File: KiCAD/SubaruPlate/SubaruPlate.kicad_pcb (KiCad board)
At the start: 2 copper layers, 140 x 140 mm, 6 parts, among them J1 Conn_01x04, U1 LPS28DFW

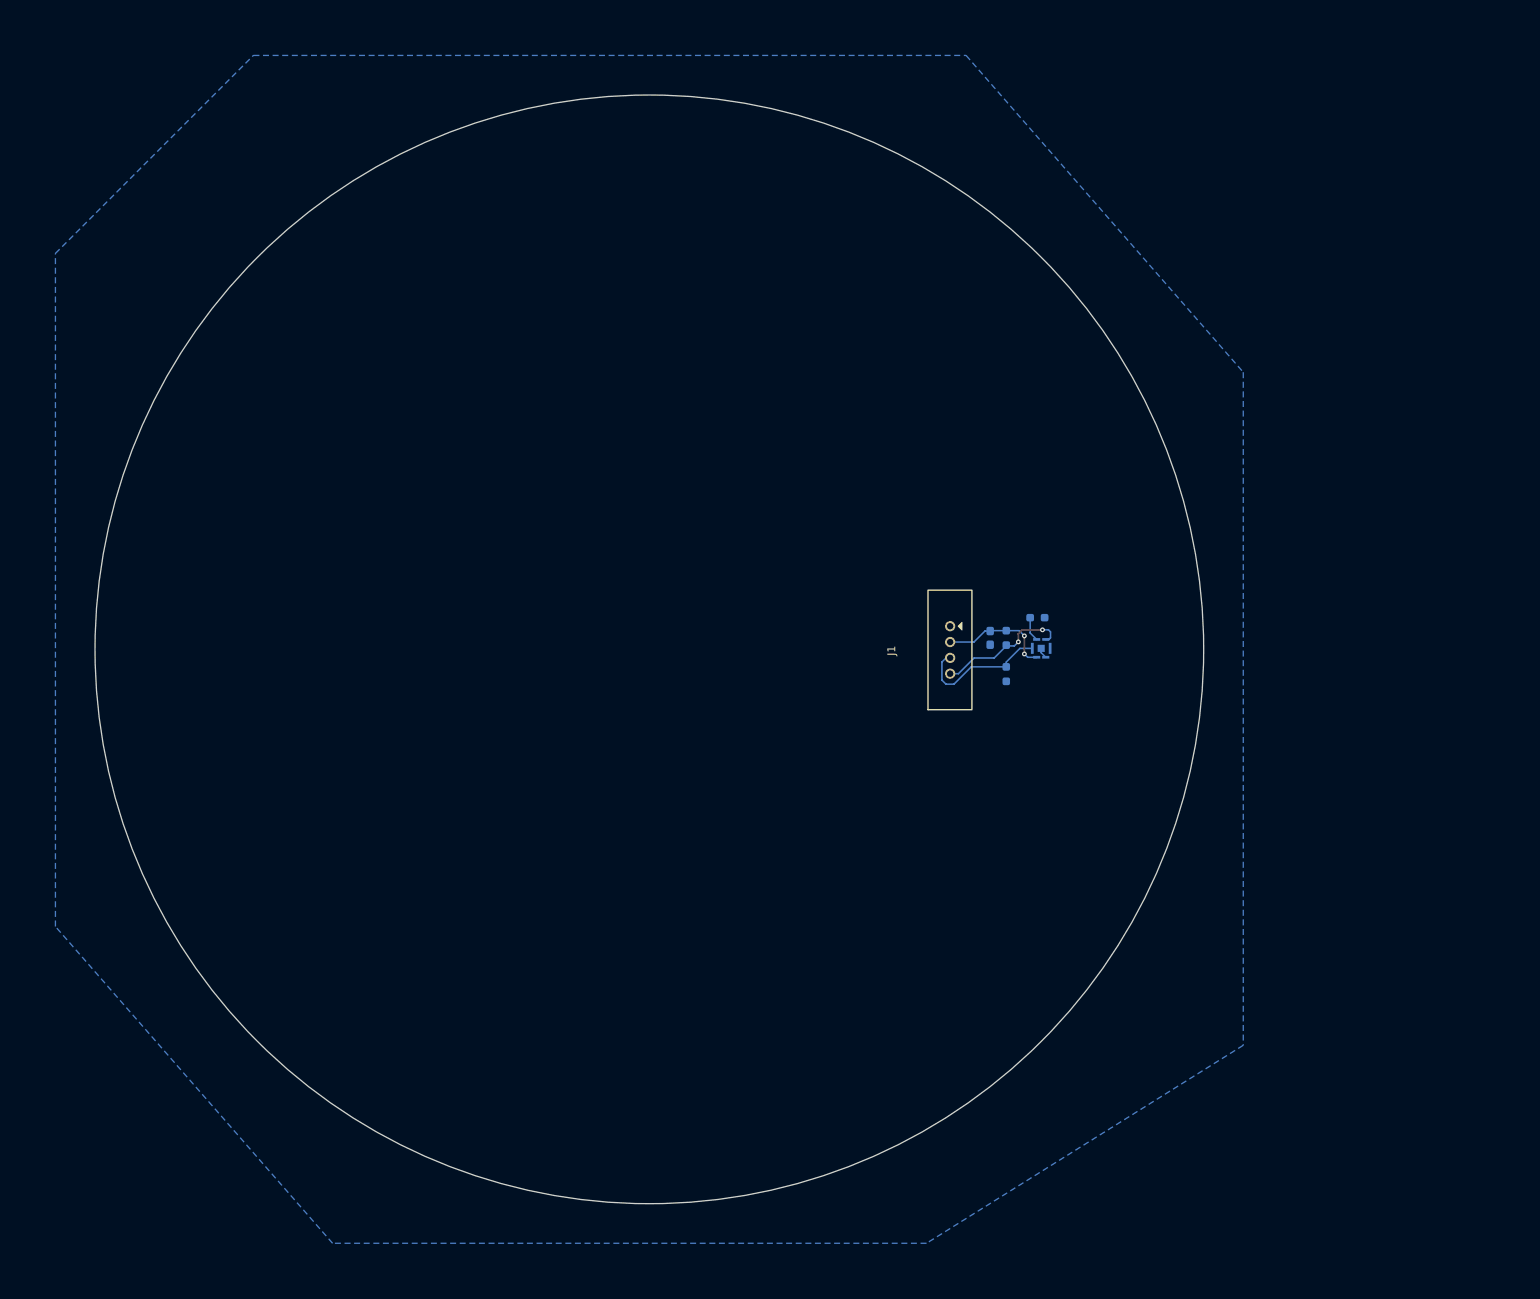
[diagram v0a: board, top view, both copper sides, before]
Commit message: Power, CanInterface, MCU, Sensorと項目に分け設計
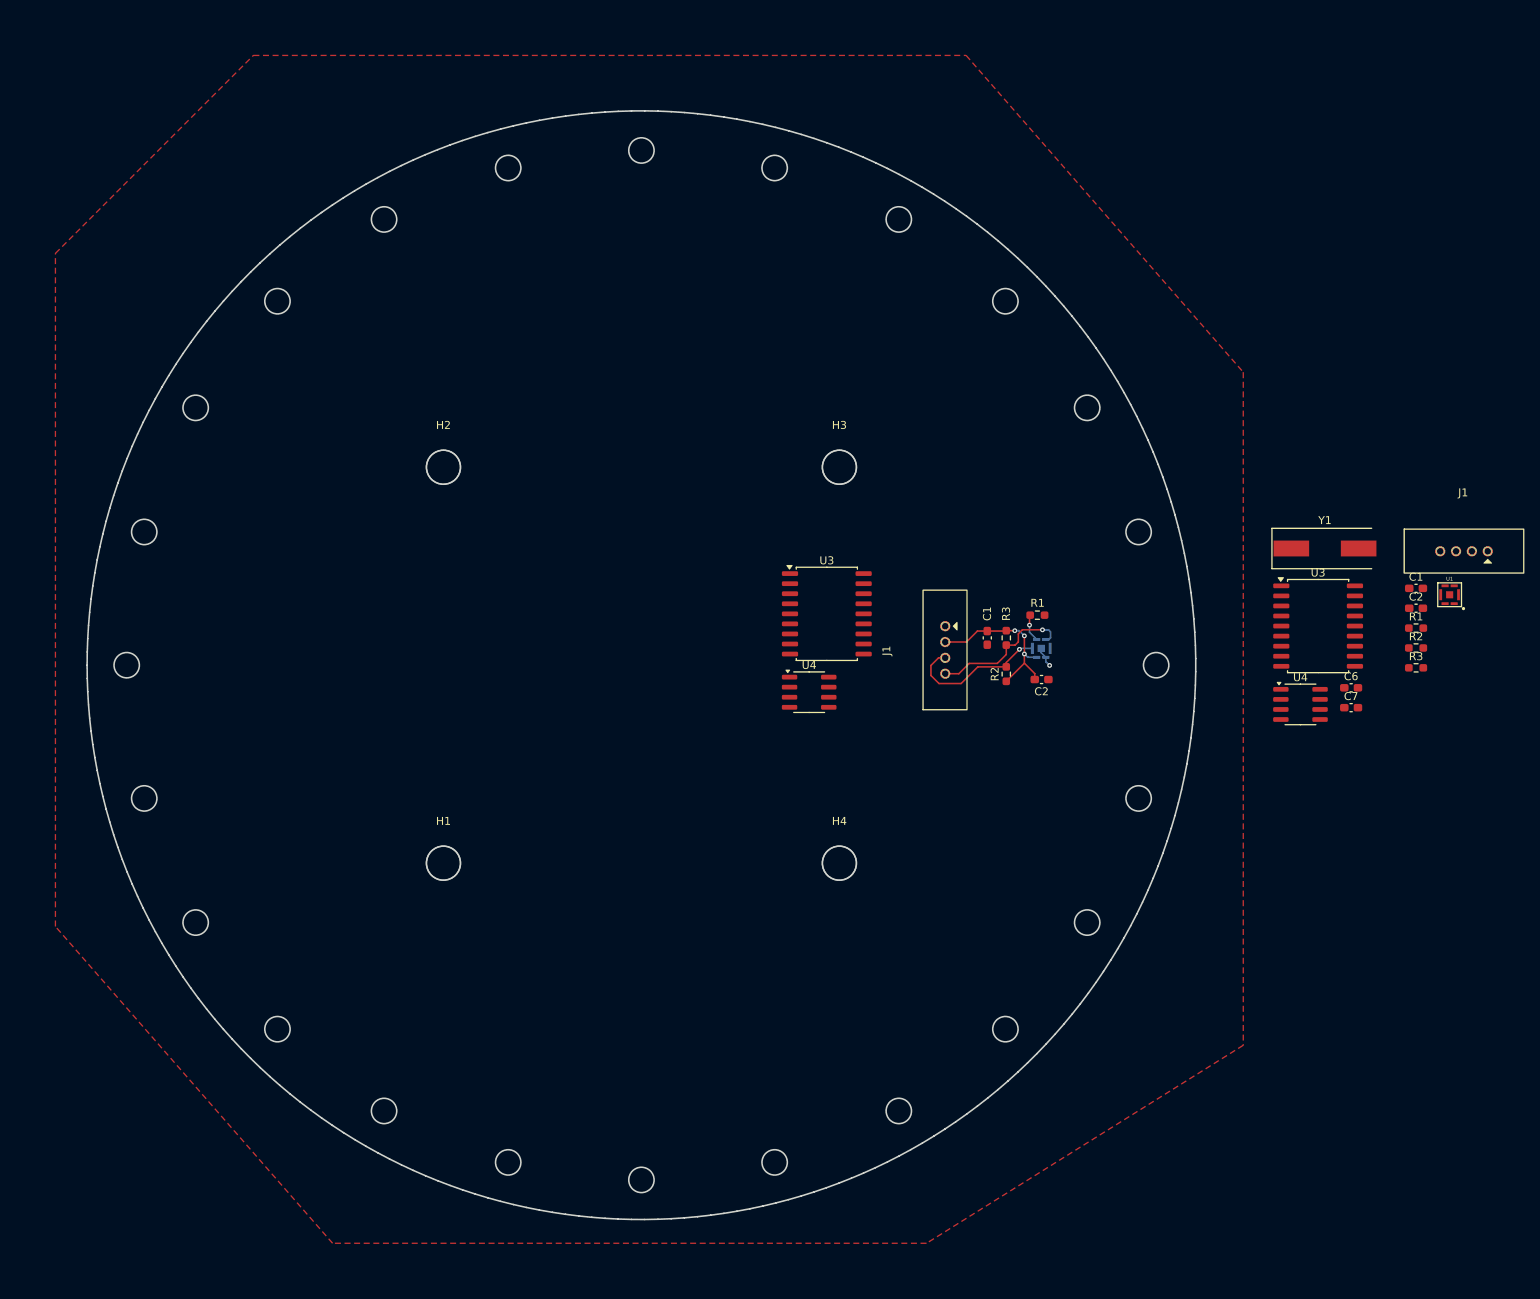
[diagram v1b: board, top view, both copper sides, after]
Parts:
- added C1: 10uF, Capacitor_SMD:C_0603_1608Metric_Pad1.08x0.95mm_HandSolder, F.Cu at (246.8, 92.3)
- added C2: 0.1uF, Capacitor_SMD:C_0603_1608Metric_Pad1.08x0.95mm_HandSolder, F.Cu at (246.8, 94.8)
- added C2: 0.1uF, Capacitor_SMD:C_0603_1608Metric_Pad1.08x0.95mm_HandSolder, F.Cu at (199.5, 103.8)
- added C6: 15pF, Capacitor_SMD:C_0603_1608Metric_Pad1.08x0.95mm_HandSolder, F.Cu at (238.6, 104.9)
- added C7: 15pF, Capacitor_SMD:C_0603_1608Metric_Pad1.08x0.95mm_HandSolder, F.Cu at (238.6, 107.4)
- added H1: MountingHole, MountingHole:MountingHole_4.3mm_M4, F.Cu at (124.0, 127.0)
- added H2: MountingHole, MountingHole:MountingHole_4.3mm_M4, F.Cu at (124.0, 77.0)
- added H3: MountingHole, MountingHole:MountingHole_4.3mm_M4, F.Cu at (174.0, 77.0)
- added H4: MountingHole, MountingHole:MountingHole_4.3mm_M4, F.Cu at (174.0, 127.0)
- added J1: DF51A-4P-2DSA, TSRP_Connector_Hirose:DF51A-4P-2DSA, F.Cu at (252.9, 90.2)
- added R1: 10K, Resistor_SMD:R_0603_1608Metric_Pad0.98x0.95mm_HandSolder, F.Cu at (246.8, 97.3)
- added R2: 10K, Resistor_SMD:R_0603_1608Metric_Pad0.98x0.95mm_HandSolder, F.Cu at (246.8, 99.8)
- added R3: 10K, Resistor_SMD:R_0603_1608Metric_Pad0.98x0.95mm_HandSolder, F.Cu at (246.8, 102.3)
- added U1: LPS28DFW, TSRP_IC:CCLGA-7L, F.Cu at (251.1, 93.1)
- added U3: MCP2515-xSO, Package_SO:SOIC-18W_7.5x11.6mm_P1.27mm, F.Cu at (172.4, 95.5)
- added U3: MCP2515-xSO, Package_SO:SOIC-18W_7.5x11.6mm_P1.27mm, F.Cu at (234.4, 97.1)
- added U4: MCP2562-E-SN, Package_SO:SOIC-8_3.9x4.9mm_P1.27mm, F.Cu at (170.2, 105.4)
- added U4: MCP2562-E-SN, Package_SO:SOIC-8_3.9x4.9mm_P1.27mm, F.Cu at (232.2, 107.0)
- added Y1: 8MHz, Crystal:Crystal_SMD_HC49-SD, F.Cu at (235.3, 87.3)
- C1: value C -> 10uF; moved to F.Cu
- J1: value Conn_01x04 -> DF51A-4P-2DSA
- R1, R2, R3: value R -> 10K; moved to F.Cu
- moved J1 0.62 mm to (190.0, 100.1)
- moved C1 0.37 mm to (192.7, 98.6)
- moved R1 0.32 mm to (199.0, 95.7)
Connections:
- J1 pad 3: I2C_SDA -> unconnected-(J1-Pin_3-Pad3)
- J1 pad 4: I2C_SCL -> unconnected-(J1-Pin_4-Pad4)
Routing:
- net +3.3V: track 14.3 -> 22.8 mm, vias 2 -> 3
- net I2C_SDA: track 17.4 -> 18.9 mm, vias 0 -> 1
- net GND: track 1.36 -> 2.60 mm, vias 0 -> 1
- net I2C_SCL: track 17.8 -> 18.4 mm, vias 2 -> 1
- net Net-(U1-SA0): track 3.09 -> 3.16 mm, vias 0 -> 1
- added copper zone on F.Cu, net GND
- removed copper zone on B.Cu, net GND
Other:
- outline, holes or cut-outs redrawn

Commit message: SubaruPlateを更新
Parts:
- removed the C1 at (246.8, 92.3)
- removed the C1 at (192.7, 98.6)
- removed the C2 at (246.8, 94.8)
- removed the C2 at (199.5, 103.8)
- removed H1, H2, H3, H4: MountingHole, MountingHole:MountingHole_4.3mm_M4
- removed the J1 at (190.0, 100.1)
- removed the J1 at (252.9, 90.2)
- removed the R1 at (199.0, 95.7)
- removed the R1 at (246.8, 97.3)
- removed the R2 at (195.1, 103.1)
- removed the R2 at (246.8, 99.8)
- removed the R3 at (195.1, 98.6)
- removed the R3 at (246.8, 102.3)
- removed the U1 at (251.1, 93.1)
- removed the U1 at (199.5, 99.9)
- removed the U3 at (172.4, 95.5)
- removed the U3 at (234.4, 97.1)
- removed the U4 at (170.2, 105.4)
- removed the U4 at (232.2, 107.0)
- added C1: 10uF, Capacitor_SMD:C_0603_1608Metric_Pad1.08x0.95mm_HandSolder, F.Cu at (189.5, 102.1)
- added C2: 0.1uF, Capacitor_SMD:C_0603_1608Metric_Pad1.08x0.95mm_HandSolder, F.Cu at (196.4, 107.6)
- added C3: 0.1uF, Capacitor_SMD:C_0603_1608Metric_Pad1.08x0.95mm_HandSolder, F.Cu at (182.5, 104.6)
- added C4: 0.1uF, Capacitor_SMD:C_0603_1608Metric_Pad1.08x0.95mm_HandSolder, F.Cu at (159.1, 134.6)
- added C5: 0.1uF, Capacitor_SMD:C_0603_1608Metric_Pad1.08x0.95mm_HandSolder, F.Cu at (169.8, 108.6)
- added H5: MountingHole_Pad, MountingHole:MountingHole_4.3mm_M4_Pad_TopBottom, F.Cu at (124.0, 77.0)
- added H6: MountingHole_Pad, MountingHole:MountingHole_4.3mm_M4_Pad_TopBottom, F.Cu at (124.0, 127.0)
- added H7: MountingHole_Pad, MountingHole:MountingHole_4.3mm_M4_Pad_TopBottom, F.Cu at (174.0, 77.0)
- added H8: MountingHole_Pad, MountingHole:MountingHole_4.3mm_M4_Pad_TopBottom, F.Cu at (174.0, 127.0)
- added J1: DF51A-4P-2DSA, TSRP_Connector_Hirose:DF51A-4P-2DSA, F.Cu at (161.4, 144.6)
- added J2: B3B-XH-A(LF)(SN), Connector_JST:JST_XH_B3B-XH-A_1x03_P2.50mm_Vertical, B.Cu at (142.8, 140.2)
- added JP1: Jumper_2_Open, Jumper:SolderJumper-2_P1.3mm_Open_TrianglePad1.0x1.5mm, F.Cu at (135.6, 104.9)
- added PS1: M78AR05-0.5, TSRP_IC:M78AR03305, F.Cu at (176.4, 148.0)
- added R1: 10K, Resistor_SMD:R_0603_1608Metric_Pad0.98x0.95mm_HandSolder, F.Cu at (196.4, 99.5)
- added R2: 10K, Resistor_SMD:R_0603_1608Metric_Pad0.98x0.95mm_HandSolder, F.Cu at (192.1, 106.5)
- added R3: 10K, Resistor_SMD:R_0603_1608Metric_Pad0.98x0.95mm_HandSolder, F.Cu at (192.1, 102.1)
- added R6: 120, Resistor_SMD:R_0603_1608Metric_Pad0.98x0.95mm_HandSolder, F.Cu at (139.2, 116.3)
- added U1: LPS28DFW, TSRP_IC:CCLGA-7L, B.Cu at (196.5, 103.8)
- added U3: MCP2515-xSO, Package_SO:SOIC-18W_7.5x11.6mm_P1.27mm, F.Cu at (164.2, 116.1)
- added U4: MCP2562-E-SN, Package_SO:SOIC-8_3.9x4.9mm_P1.27mm, F.Cu at (163.3, 131.3)
- added U5: XIAO-RP2040-DIP, Seeed_XIAO:XIAO-RP2040-SMD, F.Cu at (191.4, 121.7)
- moved C6 86.7 mm to (154.8, 127.3), turned to 180 degrees
- moved Y1 86.7 mm to (154.8, 119.5), turned to -90 degrees
- moved C7 83.9 mm to (154.8, 111.4)
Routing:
- net +12V: track 0.00 -> 25.5 mm
- net CAN_TX: track 0.00 -> 21.6 mm
- net CAN_RX: track 0.00 -> 21.5 mm
- net SPI_MOSI: track 0.00 -> 16.7 mm, vias 0 -> 2
- net SPI_MISO: track 0.00 -> 16.2 mm, vias 0 -> 2
- net I2C_SDA: track 18.9 -> 4.10 mm
- net SPI_SCK: track 0.00 -> 14.7 mm
- net CAN_H: track 0.00 -> 13.6 mm
- net CAN_L: track 0.00 -> 13.5 mm
- net +3.3V: track 22.8 -> 9.54 mm
- net I2C_SCL: track 18.4 -> 7.98 mm
- net OSC2: track 0.00 -> 10.4 mm
- net OSC1: track 0.00 -> 10.3 mm
- net GND: track 2.60 -> 1.19 mm

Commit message: 後は最終確認
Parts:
- removed J2: B3B-XH-A(LF)(SN), Connector_JST:JST_XH_B3B-XH-A_1x03_P2.50mm_Vertical
- removed JP1: Jumper_2_Open, Jumper:SolderJumper-2_P1.3mm_Open_TrianglePad1.0x1.5mm
- removed PS1: M78AR05-0.5, TSRP_IC:M78AR03305
- added BZ1: Buzzer, Buzzer_Beeper:Buzzer_12x9.5RM7.6, B.Cu at (150.0, 103.8)
- added C11: 22u, Capacitor_SMD:C_0805_2012Metric_Pad1.18x1.45mm_HandSolder, F.Cu at (131.0, 139.7)
- added C12: 10u, Capacitor_SMD:C_0805_2012Metric_Pad1.18x1.45mm_HandSolder, F.Cu at (131.0, 135.4)
- added C8: 1u, Capacitor_SMD:C_0603_1608Metric_Pad1.08x0.95mm_HandSolder, F.Cu at (149.9, 132.6)
- added C9: 1u, Capacitor_SMD:C_0603_1608Metric_Pad1.08x0.95mm_HandSolder, F.Cu at (156.4, 133.4)
- added MD2: OKL-T_6-W12N-C, TSRP_IC:MURATA_OKL-T-6-W12N-C_0, F.Cu at (141.0, 138.7)
- added Q1: NMOS, Package_TO_SOT_SMD:SOT-23, F.Cu at (147.6, 90.2)
- added R10: 1k 0.1%, Resistor_SMD:R_0603_1608Metric_Pad0.98x0.95mm_HandSolder, F.Cu at (145.6, 129.1)
- added R11: 330 0.1%, Resistor_SMD:R_0603_1608Metric_Pad0.98x0.95mm_HandSolder, F.Cu at (143.6, 129.1)
- added R12: 10 0.1%, Resistor_SMD:R_0603_1608Metric_Pad0.98x0.95mm_HandSolder, F.Cu at (141.5, 129.1)
- added R13: 600, Resistor_SMD:R_0603_1608Metric_Pad0.98x0.95mm_HandSolder, F.Cu at (149.9, 108.8)
- added R4: 10K, Resistor_SMD:R_0603_1608Metric_Pad0.98x0.95mm_HandSolder, F.Cu at (173.3, 112.8)
- added R5: 750, Resistor_SMD:R_0603_1608Metric_Pad0.98x0.95mm_HandSolder, F.Cu at (152.7, 91.2)
- added R7: 10k, Resistor_SMD:R_0603_1608Metric_Pad0.98x0.95mm_HandSolder, F.Cu at (152.7, 89.2)
- added R8: 20k, Resistor_SMD:R_0603_1608Metric_Pad0.98x0.95mm_HandSolder, F.Cu at (137.7, 147.4)
- added R9: 100k, Resistor_SMD:R_0603_1608Metric_Pad0.98x0.95mm_HandSolder, F.Cu at (132.1, 130.3)
- added U2: NCV8114BSN330T1G, Package_TO_SOT_SMD:TSOT-23-5, F.Cu at (153.2, 135.7)
- H5, H6, H7, H8: footprint MountingHole:MountingHole_4.3mm_M4_Pad_TopBottom -> MountingHole:MountingHole_3.2mm_M3_Pad_TopBottom
- moved R6 33.3 mm to (163.4, 139.2)
- moved U5 31.4 mm to (170.4, 98.5), turned to -90 degrees
- moved C5 19.1 mm to (163.4, 126.5)
- moved C3 13.7 mm to (171.5, 112.8), turned to 90 degrees
- moved R1 9.31 mm to (191.6, 107.5)
- moved C1 9.31 mm to (184.7, 110.0)
- moved R2 9.31 mm to (187.2, 114.5)
- moved R3 9.31 mm to (187.2, 110.0)
- moved U1 9.31 mm to (191.7, 111.7)
- moved C2 9.10 mm to (191.6, 115.4)
- moved J1 4.15 mm to (161.4, 140.4)
- moved C6 2.83 mm to (154.8, 130.1)
- moved C7 2.83 mm to (154.8, 114.2)
- moved U3 2.83 mm to (164.2, 118.9)
- moved Y1 2.83 mm to (154.8, 122.3)
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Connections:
- R6 pad 2: Net-(JP1-B) -> CAN_H
- U5 pad 12: +3.3V -> unconnected-(U5-3V3-Pad12)
- U5 pad 3: unconnected-(U5-GPIO28/ADC2/A2-Pad3) -> Buzzer
- U5 pad 4: unconnected-(U5-GPIO29/ADC3/A3-Pad4) -> SPI_CS_MCP2515
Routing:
- net +5V: track 0.00 -> 79.6 mm, vias 0 -> 4
- net +3.3V: track 9.54 -> 69.4 mm, vias 3 -> 6
- net +12V: track 25.5 -> 81.2 mm, vias 0 -> 2
- net I2C_SCL: track 7.98 -> 43.7 mm, vias 1 -> 3
- net I2C_SDA: track 4.10 -> 37.9 mm, vias 1 -> 3
- net SPI_CS_MCP2515: track 0.00 -> 29.0 mm, vias 0 -> 2
- net Buzzer: track 0.00 -> 25.1 mm
- net P.G._OKL-T/6-W12N-C: track 0.00 -> 20.8 mm, vias 0 -> 2
- net SPI_SCK: track 14.7 -> 25.1 mm, vias 0 -> 2
- net CAN_H: track 13.6 -> 5.57 mm
- net CAN_L: track 13.5 -> 5.53 mm
- net SPI_MISO: track 16.2 -> 23.5 mm, vias 2 -> 0
- net SPI_MOSI: track 16.7 -> 23.5 mm, vias 2 -> 0
- net CAN_RX: track 21.5 -> 15.1 mm
- net Net-(BZ1--): track 0.00 -> 6.09 mm
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- added copper zone on F.Cu, net +12V
- added copper zone on F.Cu, net +5V
- added copper zone on B.Cu, net GND
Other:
- outline, holes or cut-outs redrawn
- board text added: "Lug"
